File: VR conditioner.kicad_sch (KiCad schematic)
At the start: 15 parts, among them U3 MAX9924

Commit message: updated and fixed, check JLC exports
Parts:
- C4, C5: footprint Capacitor_SMD:C_0603_1608Metric -> Capacitor_SMD:C_0805_2012Metric
- C6: footprint Capacitor_SMD:C_0603_1608Metric -> Capacitor_SMD:C_0805_2012Metric_Pad1.18x1.45mm_HandSolder
- R7, R8: footprint Resistor_SMD:R_0402_1005Metric -> Resistor_SMD:R_0805_2012Metric
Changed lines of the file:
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@@
       (effects (font (size 1.27 1.27)) (justify left))
     )
-    (property "Footprint" "Capacitor_SMD:C_0603_1608Metric" (id 2) (at 120.3452 90.17 0)
+    (property "Footprint" "Capacitor_SMD:C_0805_2012Metric" (id 2) (at 120.3452 90.17 0)
       (effects (font (size 1.27 1.27)) hide)
     )
@@
     (property "Reference" "R7" (id 0) (at 128.27 97.155 90))
     (property "Value" "1k" (id 1) (at 128.27 99.06 90))
-    (property "Footprint" "Resistor_SMD:R_0402_1005Metric" (id 2) (at 128.27 100.838 90)
+    (property "Footprint" "Resistor_SMD:R_0805_2012Metric" (id 2) (at 128.27 100.838 90)
       (effects (font (size 1.27 1.27)) hide)
     )
@@
     (property "Reference" "C5" (id 0) (at 123.19 114.3 90))
     (property "Value" "1u" (id 1) (at 128.27 114.3 90))
-    (property "Footprint" "Capacitor_SMD:C_0603_1608Metric" (id 2) (at 124.46 112.0902 0)
+    (property "Footprint" "Capacitor_SMD:C_0805_2012Metric" (id 2) (at 124.46 112.0902 0)
       (effects (font (size 1.27 1.27)) hide)
     )
@@
       (effects (font (size 1.27 1.27)) (justify left))
     )
-    (property "Footprint" "Capacitor_SMD:C_0603_1608Metric" (id 2) (at 190.8302 108.585 0)
+    (property "Footprint" "Capacitor_SMD:C_0805_2012Metric_Pad1.18x1.45mm_HandSolder" (id 2) (at 190.8302 108.585 0)
       (effects (font (size 1.27 1.27)) hide)
     )
@@
     (property "Reference" "R8" (id 0) (at 128.27 102.87 90))
     (property "Value" "1k" (id 1) (at 128.27 104.775 90))
-    (property "Footprint" "Resistor_SMD:R_0402_1005Metric" (id 2) (at 128.27 106.553 90)
-      (effects (font (size 1.27 1.27)) hide)
-    )
+    (property "Footprint" "Resistor_SMD:R_0805_2012Metric" (id 2) (at 128.27 106.553 90)
+      (effects (font (size 1.27 1.27)) hide)
+    )

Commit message: All fixed up for JLC
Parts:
- C4: LCSC C1588 -> C46653
- C5: LCSC C15849 -> C28323
- C6: LCSC C14663 -> C28323
- R7, R8: LCSC C11702 -> C17513
- U3: LCSC N/A -> C143633
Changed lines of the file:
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@@
       (effects (font (size 1.27 1.27)) hide)
     )
-    (property "LCSC" "C1588" (id 4) (at 119.38 86.36 0)
+    (property "LCSC" "C46653" (id 4) (at 119.38 86.36 0)
       (effects (font (size 1.27 1.27)) hide)
     )
@@
       (effects (font (size 1.27 1.27)) hide)
     )
-    (property "LCSC" "N/A" (id 4) (at 151.13 91.44 0)
+    (property "LCSC" "C143633" (id 4) (at 151.13 91.44 0)
       (effects (font (size 1.27 1.27)) hide)
     )
@@
       (effects (font (size 1.27 1.27)) hide)
     )
-    (property "LCSC" "C11702" (id 4) (at 128.27 99.06 0)
+    (property "LCSC" "C17513" (id 4) (at 128.27 99.06 0)
       (effects (font (size 1.27 1.27)) hide)
     )
@@
       (effects (font (size 1.27 1.27)) hide)
     )
-    (property "LCSC" "C15849" (id 4) (at 128.27 111.125 0)
+    (property "LCSC" "C28323" (id 4) (at 128.27 111.125 0)
       (effects (font (size 1.27 1.27)) hide)
     )
@@
       (effects (font (size 1.27 1.27)) hide)
     )
-    (property "LCSC" "C14663" (id 4) (at 189.865 104.775 0)
+    (property "LCSC" "C28323" (id 4) (at 189.865 104.775 0)
       (effects (font (size 1.27 1.27)) hide)
     )
@@
       (effects (font (size 1.27 1.27)) hide)
     )
-    (property "LCSC" "C11702" (id 4) (at 128.27 104.775 0)
-      (effects (font (size 1.27 1.27)) hide)
-    )
+    (property "LCSC" "C17513" (id 4) (at 128.27 104.775 0)
+      (effects (font (size 1.27 1.27)) hide)
+    )

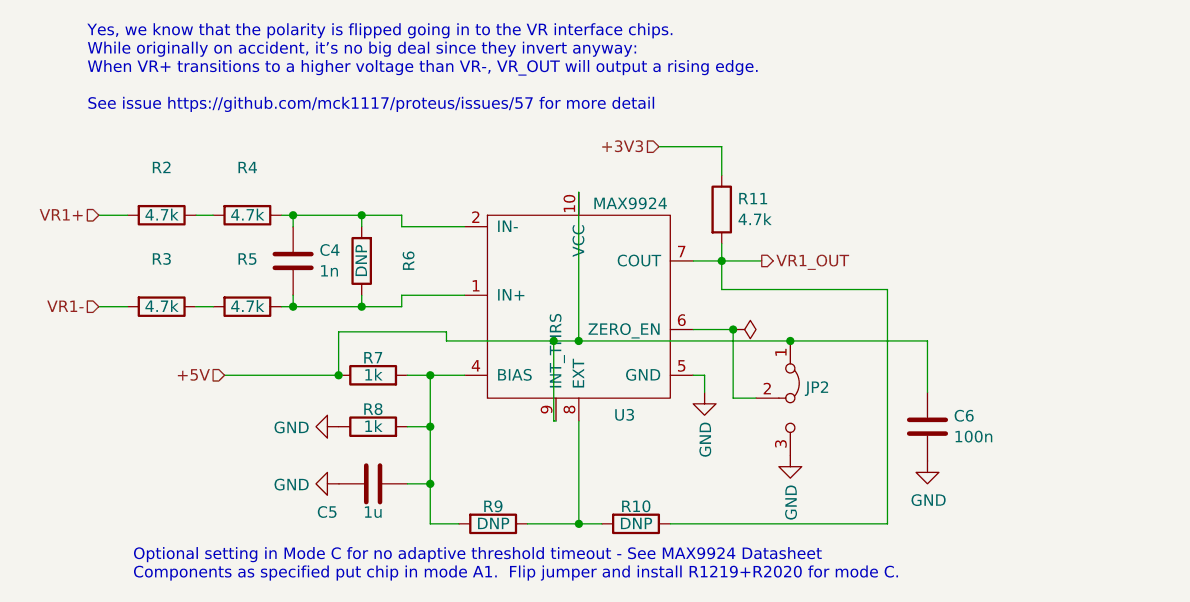
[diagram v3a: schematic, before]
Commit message: fix wideband library, ERC, DRC
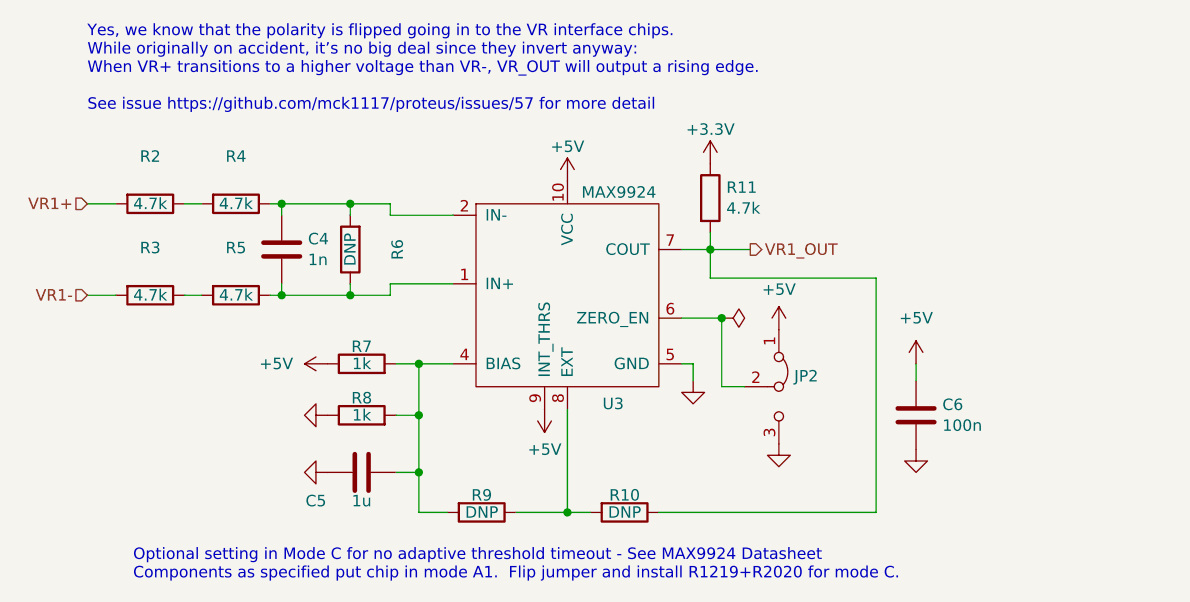
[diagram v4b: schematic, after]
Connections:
- net +3V3 renamed +3.3V
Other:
- moved on the sheet: C4, C5, C6, JP2, R10, R11, R2, R3, R4, R5, R6, R7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

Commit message: Add freewheel diodes, power pins explanation comment
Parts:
- R10, R9: footprint Simon:R_0805_2012Metric_Pad1.15x1.40mm_HandSolder -> Resistor_SMD:R_0805_2012Metric_Pad1.20x1.40mm_HandSolder
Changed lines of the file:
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@@
       (effects (font (size 1.27 1.27)))
     )
-    (property "Footprint" "Simon:R_0805_2012Metric_Pad1.15x1.40mm_HandSolder" (at 142.113 114.3 90)
+    (property "Footprint" "Resistor_SMD:R_0805_2012Metric_Pad1.20x1.40mm_HandSolder" (at 142.113 114.3 90)
       (effects (font (size 1.27 1.27)) hide)
     )
@@
       (effects (font (size 1.27 1.27)))
     )
-    (property "Footprint" "Simon:R_0805_2012Metric_Pad1.15x1.40mm_HandSolder" (at 157.988 114.3 90)
-      (effects (font (size 1.27 1.27)) hide)
-    )
+    (property "Footprint" "Resistor_SMD:R_0805_2012Metric_Pad1.20x1.40mm_HandSolder" (at 157.988 114.3 90)
+      (effects (font (size 1.27 1.27)) hide)
+    )

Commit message: schematic title blocks
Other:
- company: (none) -> FutureProofPerformance.com
- title: (none) -> Polygonus Universal 88p
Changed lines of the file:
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@@
 (kicad_sch (version 20230121) (generator eeschema)
   (paper "A4")
+  (title_block
+    (title "Polygonus Universal 88p")
+    (date "2023-11-12")
+    (rev "v1.0")
+    (company "FutureProofPerformance.com")
+  )
   (junction (at 125.73 90.17) (diameter 0) (color 0 0 0 0)
   )
